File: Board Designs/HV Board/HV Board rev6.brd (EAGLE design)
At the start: 147.3 x 71.1 mm, 65 parts, among them IC1 OKI-78SR, IC2 NE5532SOIC

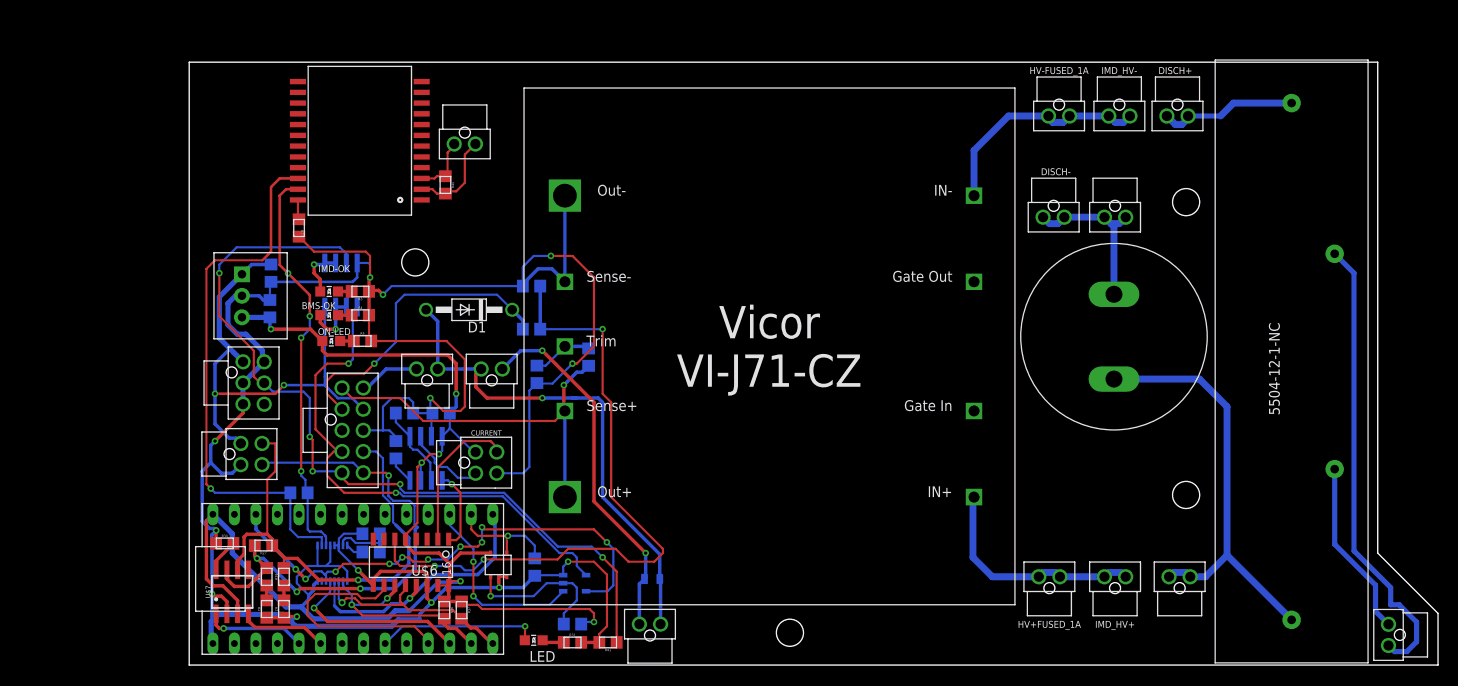
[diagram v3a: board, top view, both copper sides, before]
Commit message: Fixed 6820 distance for rev6
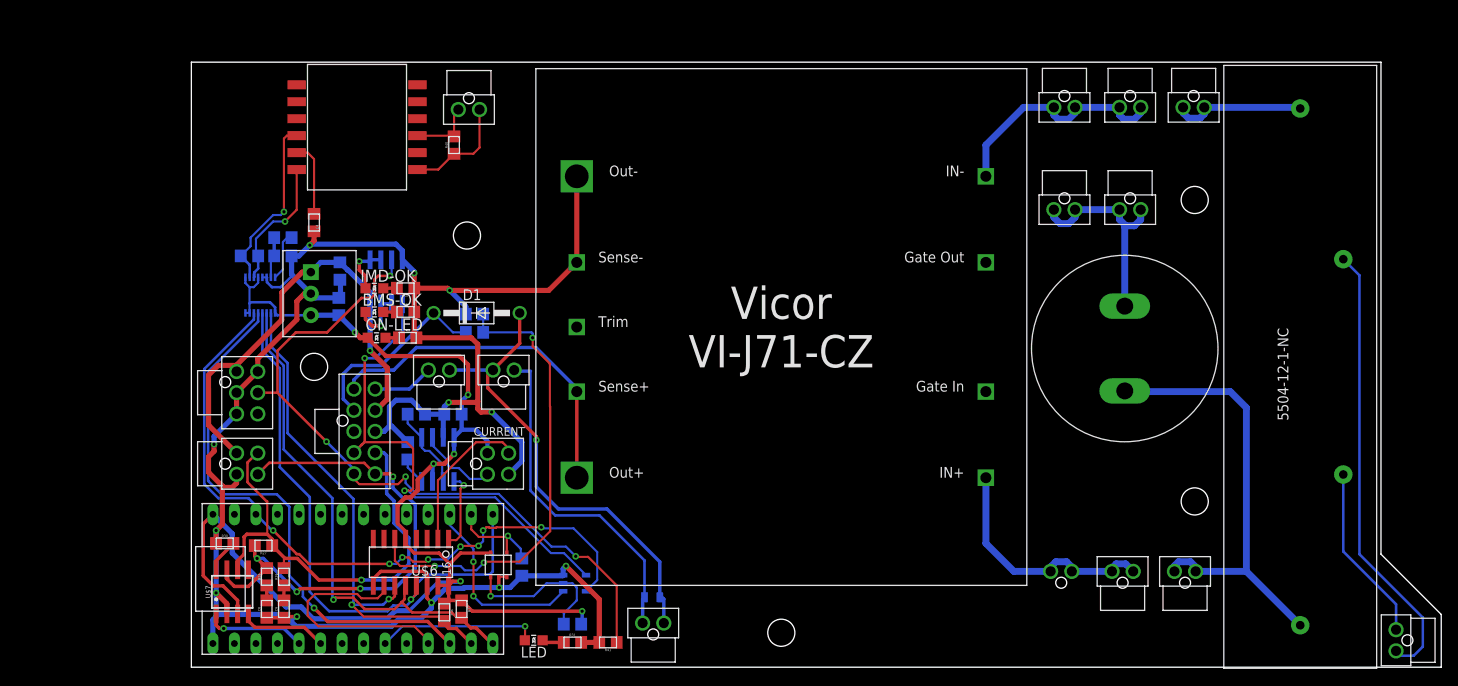
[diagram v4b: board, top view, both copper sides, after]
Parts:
- removed TRIM+, TRIM-: (no value), HyTechDevices:0805
- U$2: value SM51589PEL -> HM2102NLT; device HyTechDevices:SM51589PEL -> HyTechDevices:HM2102NLT
- moved R33 38.5 mm to (31.4, 45.3), turned to 0 degrees
- moved R34 34.4 mm to (31.4, 43.2), turned to 180 degrees
- moved U$8 32.7 mm to (30.4, 37.0)
- moved R35 28.5 mm to (27.4, 43.2)
- moved C2 8.13 mm to (38.1, 41.4)
- moved C3 8.13 mm to (38.0, 37.2)
- moved IC1 8.13 mm to (34.7, 38.7)
- moved R2 7.50 mm to (54.0, 36.3)
- moved R1 6.74 mm to (54.0, 34.2)
- moved BMS-OK 5.35 mm to (42.2, 36.6)
- moved IC2 5.35 mm to (43.6, 40.1)
- moved IMD-OK 5.35 mm to (42.2, 39.4)
- moved R3 5.35 mm to (45.8, 39.4)
- moved R4 5.35 mm to (45.8, 36.6)
- moved ON-LED 5.35 mm to (42.4, 33.5)
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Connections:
- removed net TRIM: TRIM+.1, TRIM-.1, U$5.7TRIM
- net GND: no longer TRIM-.2
- net ISOSPI-M: now also R40.2, U$2.P$3; no longer R40.1, U$2.3
- net ISOSPI-P: now also R40.1, U$2.P$1; no longer R40.2, U$2.2
- net N$33: now also U$2.P$10; no longer U$2.22
- net N$34: now also U$2.P$12; no longer U$2.23
- net N$35: now also U$2.P$11; no longer U$2.24
- net TSAL+: no longer TRIM+.2
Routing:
- net GND: track 311.7 -> 258.7 mm, vias 13 -> 12
- net N$33: track 64.8 -> 21.1 mm
- net CS_LTC6820: track 21.7 -> 64.0 mm
- net SCK: track 31.8 -> 69.1 mm
- net MOSI: track 26.0 -> 61.5 mm
- net MISO: track 25.7 -> 61.2 mm
- net N$34: track 47.6 -> 15.8 mm, vias 4 -> 1
- net N$24: track 79.6 -> 55.5 mm
- net +3V3: track 60.4 -> 82.9 mm, vias 10 -> 8
- net SHUTDOWN7_EXT_OUT: track 36.4 -> 23.2 mm, vias 1 -> 0
- net +5V: track 172.4 -> 159.3 mm
- net OKHS: track 98.3 -> 85.2 mm, vias 5 -> 4
- net TRIM: track 7.14 -> 0.00 mm
- net N$35: track 2.33 -> 8.84 mm
- net SHUTDOWN7: track 114.7 -> 108.9 mm
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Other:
- board size 147.3 x 71.1 mm -> 147.4 x 71.4 mm
- board text added: "2019_hv_board_rev7"
- board text added: "DISCHARGE+"
- board text added: "DISCHARGE-"
- board text added: "FUSED+"
- board text added: "FUSED-"
- board text added: "IMD"
- board text added: "IMD+"
- board text added: "IMD-"
- board text removed: "2019_hv_board_rev6"

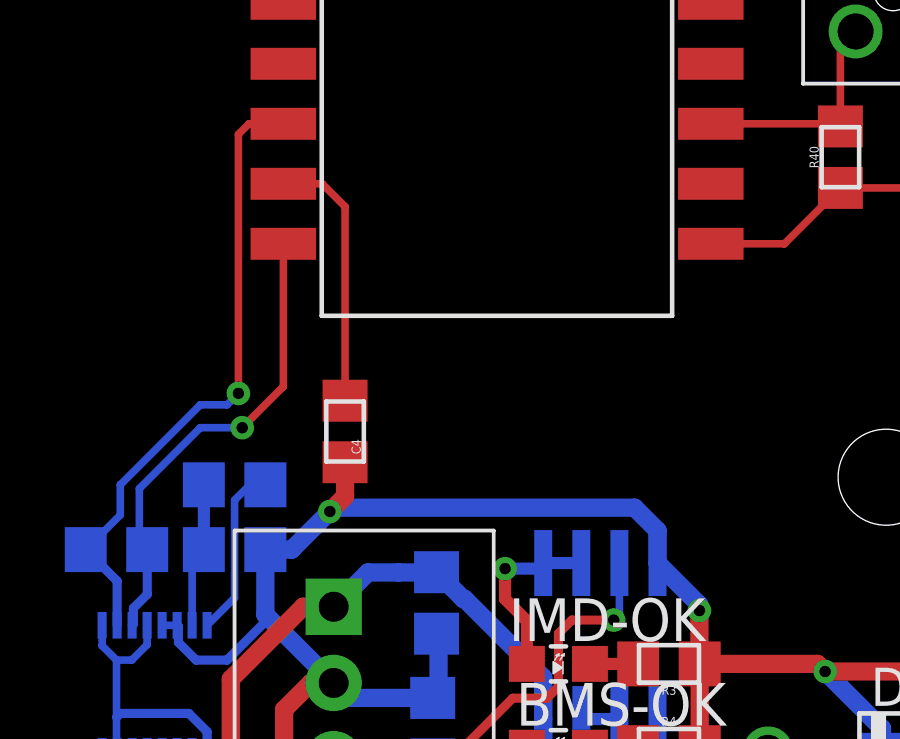
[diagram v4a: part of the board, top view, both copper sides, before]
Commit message: Moved resistor to clear space for the box
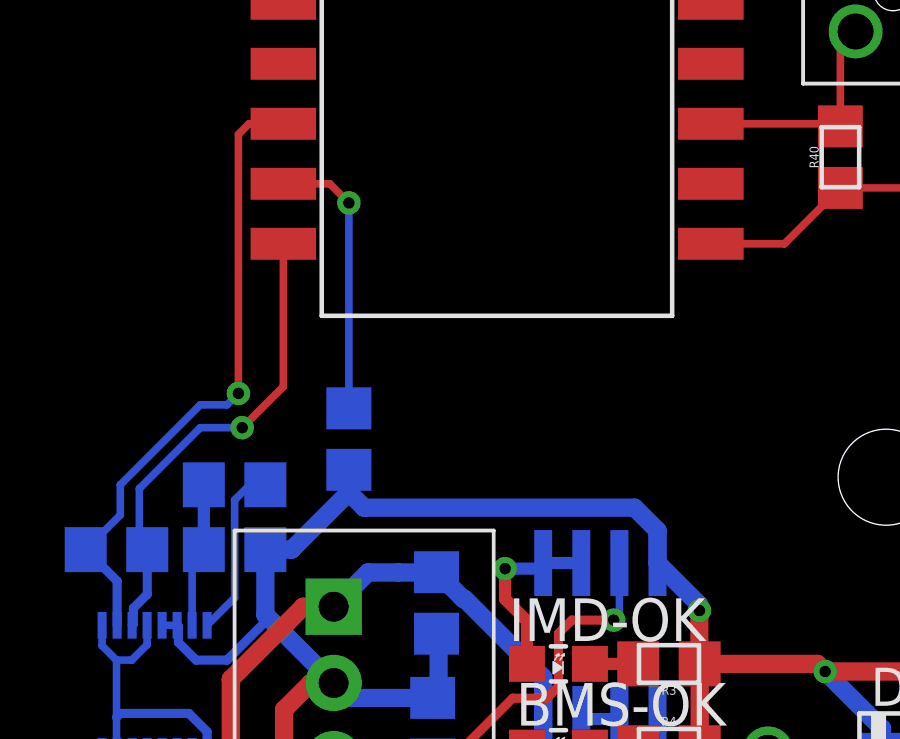
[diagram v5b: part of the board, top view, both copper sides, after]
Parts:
- moved C4 0.28 mm to (35.2, 46.9), flipped to the bottom
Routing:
- net GND: track 258.7 -> 258.0 mm, vias 12 -> 11
- net N$35: track 8.84 -> 9.30 mm, vias 0 -> 1
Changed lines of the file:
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@@
 <attribute name="VALUE" x="27.432" y="43.8912" size="0.3048" layer="28" rot="MR180" align="top-center"/>
 </element>
-<element name="C4" library="HyTechDevices" package="0805" value="27pF" x="35.052" y="47.117" smashed="yes" rot="R270">
-<attribute name="NAME" x="35.2679" y="46.609" size="0.3048" layer="25" rot="R270" align="bottom-center"/>
-<attribute name="VALUE" x="34.3408" y="47.117" size="0.3048" layer="27" rot="R270" align="top-center"/>
+<element name="C4" library="HyTechDevices" package="0805" value="27pF" x="35.179" y="46.863" smashed="yes" rot="MR270">
+<attribute name="NAME" x="34.9631" y="46.355" size="0.3048" layer="26" rot="MR270" align="bottom-center"/>
+<attribute name="VALUE" x="35.8902" y="46.863" size="0.3048" layer="28" rot="MR270" align="top-center"/>
 </element>
 <element name="R36" library="HyTechDevices" package="0805" value="2k" x="50.419" y="1.143" smashed="yes" rot="R270">
@@
 <wire x1="31.115" y1="39.497" x2="32.394" y2="40.776" width="0.3048" layer="16"/>
 <wire x1="32.394" y1="40.776" x2="32.394" y2="41.012" width="0.3048" layer="16"/>
-<wire x1="32.394" y1="43.18" x2="33.274" y2="43.18" width="0.6096" layer="16"/>
-<wire x1="33.274" y1="43.18" x2="34.544" y2="44.45" width="0.6096" layer="16"/>
-<via x="34.544" y="44.45" extent="1-16" drill="0.381"/>
-<wire x1="34.544" y1="44.45" x2="35.052" y2="44.958" width="0.6096" layer="1"/>
-<wire x1="35.052" y1="44.958" x2="35.052" y2="46.092" width="0.6096" layer="1"/>
+<wire x1="33.274" y1="43.18" x2="32.394" y2="43.18" width="0.6096" layer="16"/>
 <wire x1="45.466" y1="42.732" x2="45.466" y2="43.815" width="0.6096" layer="16"/>
 <wire x1="45.466" y1="43.815" x2="44.704" y2="44.577" width="0.6096" layer="16"/>
-<wire x1="44.704" y1="44.577" x2="34.671" y2="44.577" width="0.6096" layer="16"/>
-<wire x1="34.671" y1="44.577" x2="34.544" y2="44.45" width="0.6096" layer="16"/>
 <wire x1="45.466" y1="42.732" x2="46.863" y2="41.335" width="0.6096" layer="16"/>
 <wire x1="46.863" y1="41.335" x2="46.863" y2="41.148" width="0.6096" layer="16"/>
@@
 <wire x1="57.999" y1="17.419" x2="59.563" y2="18.983" width="0.6096" layer="16"/>
 <wire x1="59.563" y1="18.983" x2="59.563" y2="21.209" width="0.6096" layer="16"/>
+<wire x1="35.179" y1="45.838" x2="35.179" y2="45.085" width="0.6096" layer="16"/>
+<wire x1="35.179" y1="45.085" x2="33.274" y2="43.18" width="0.6096" layer="16"/>
+<wire x1="44.704" y1="44.577" x2="35.687" y2="44.577" width="0.6096" layer="16"/>
+<wire x1="35.687" y1="44.577" x2="35.179" y2="45.085" width="0.6096" layer="16"/>
 </signal>
 <signal name="+12V">
@@
 <contactref element="C4" pad="1"/>
 <contactref element="U$2" pad="P$11"/>
-<wire x1="34.29" y1="55.372" x2="35.052" y2="54.61" width="0.254" layer="1"/>
-<wire x1="35.052" y1="48.142" x2="35.052" y2="54.61" width="0.254" layer="1"/>
-<wire x1="32.994" y1="55.373" x2="34.289" y2="55.373" width="0.254" layer="1"/>
-<wire x1="34.289" y1="55.373" x2="34.29" y2="55.372" width="0.254" layer="1"/>
+<wire x1="32.994" y1="55.373" x2="34.543" y2="55.373" width="0.254" layer="1"/>
+<wire x1="34.543" y1="55.373" x2="35.179" y2="54.737" width="0.254" layer="1"/>
+<via x="35.179" y="54.737" extent="1-16" drill="0.381"/>
+<wire x1="35.179" y1="54.737" x2="35.179" y2="47.888" width="0.254" layer="16"/>
 </signal>
 <signal name="N$36">

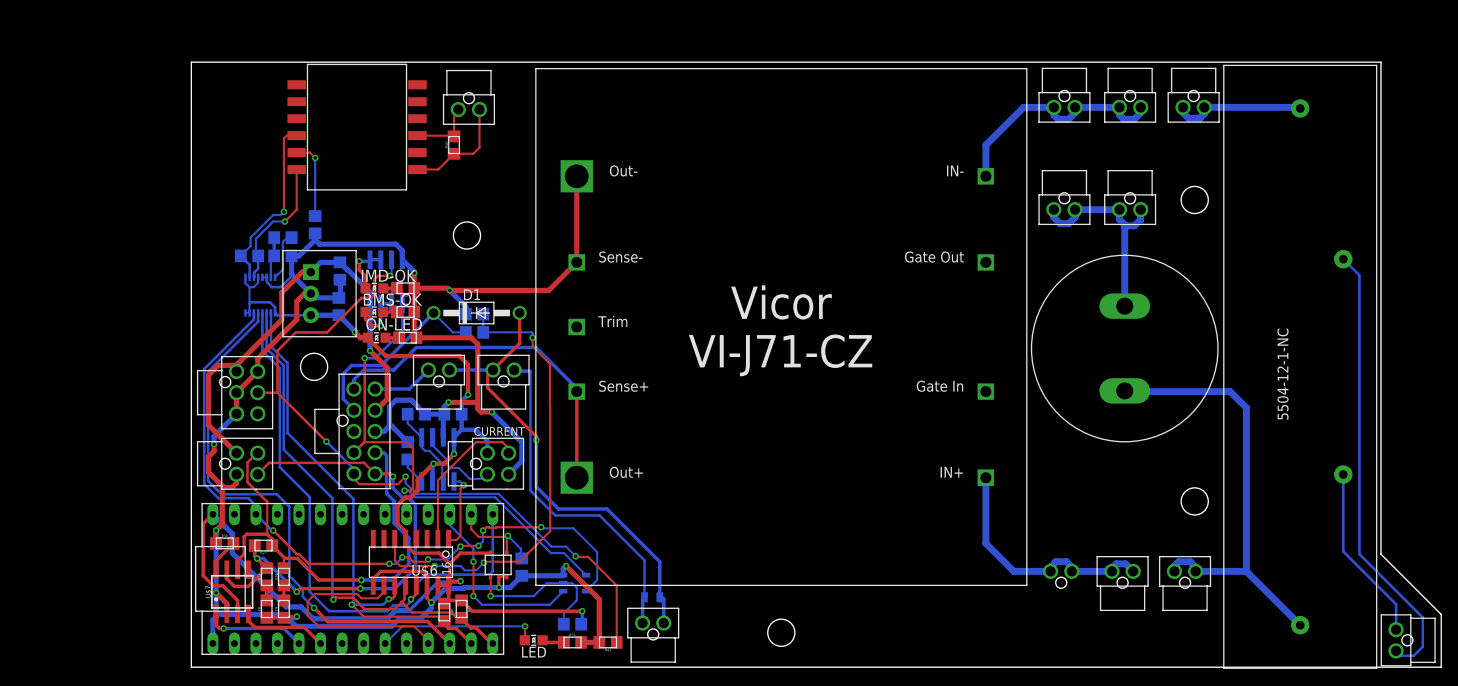
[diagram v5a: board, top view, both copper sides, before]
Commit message: Tweak HV board rev{6,7} for manufacturing
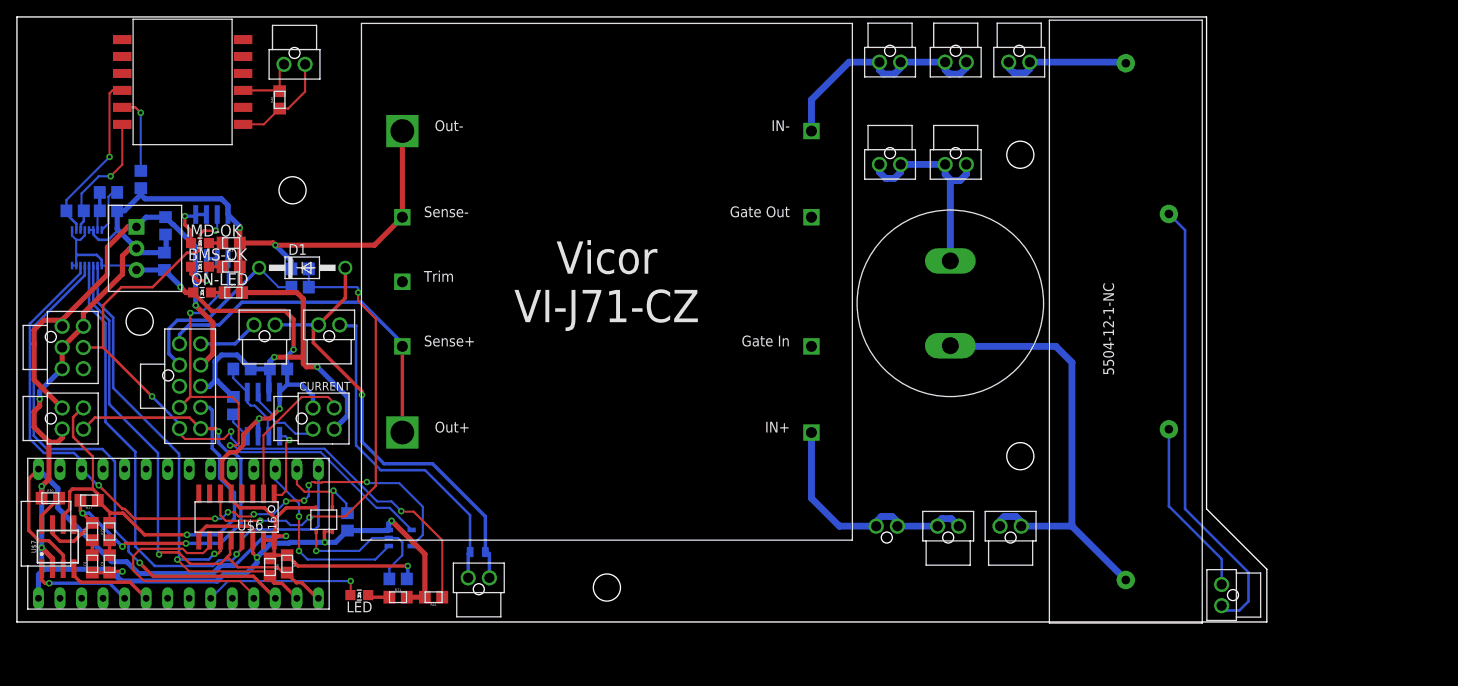
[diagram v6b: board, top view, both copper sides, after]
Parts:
- moved DISCH+ 21.3 mm to (118.2, 66.0)
- moved HV-UNFUSED 21.3 mm to (110.7, 54.0)
- moved IMD_HV- 21.3 mm to (110.7, 66.0)
- moved RELAY 21.3 mm to (142.1, 3.17)
- moved CURRENT 21.3 mm to (34.9, 24.0)
- moved D2 21.3 mm to (54.4, 8.26)
- moved R42 21.3 mm to (39.0, 11.8)
- moved RELAYS 21.3 mm to (36.8, 35.1)
- moved RELAY_JUMP 21.3 mm to (54.5, 5.21)
- moved U$9 21.3 mm to (36.8, 1.52)
- moved BMS-OK 21.3 mm to (21.6, 41.9)
- moved C2 21.3 mm to (17.5, 46.7)
- moved C4 21.3 mm to (14.6, 52.2)
- moved C5 21.3 mm to (30.9, 29.8)
- moved IC2 21.3 mm to (23.0, 45.5)
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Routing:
- net ISOSPI-P: track 12.9 -> 12.1 mm
- net N$33: track 21.1 -> 20.3 mm
- net GND: track 258.0 -> 257.3 mm
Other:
- board text added: "2019_hv_board_rev6"
- board text removed: "2019_hv_board_rev7"
